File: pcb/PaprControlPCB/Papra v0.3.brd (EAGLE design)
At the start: 30 x 45 mm, 32 parts, among them Q1 AO3400A (C20917), U1 LP2985-50DBVR (C74511), U2 ATTINYX04SOIC14

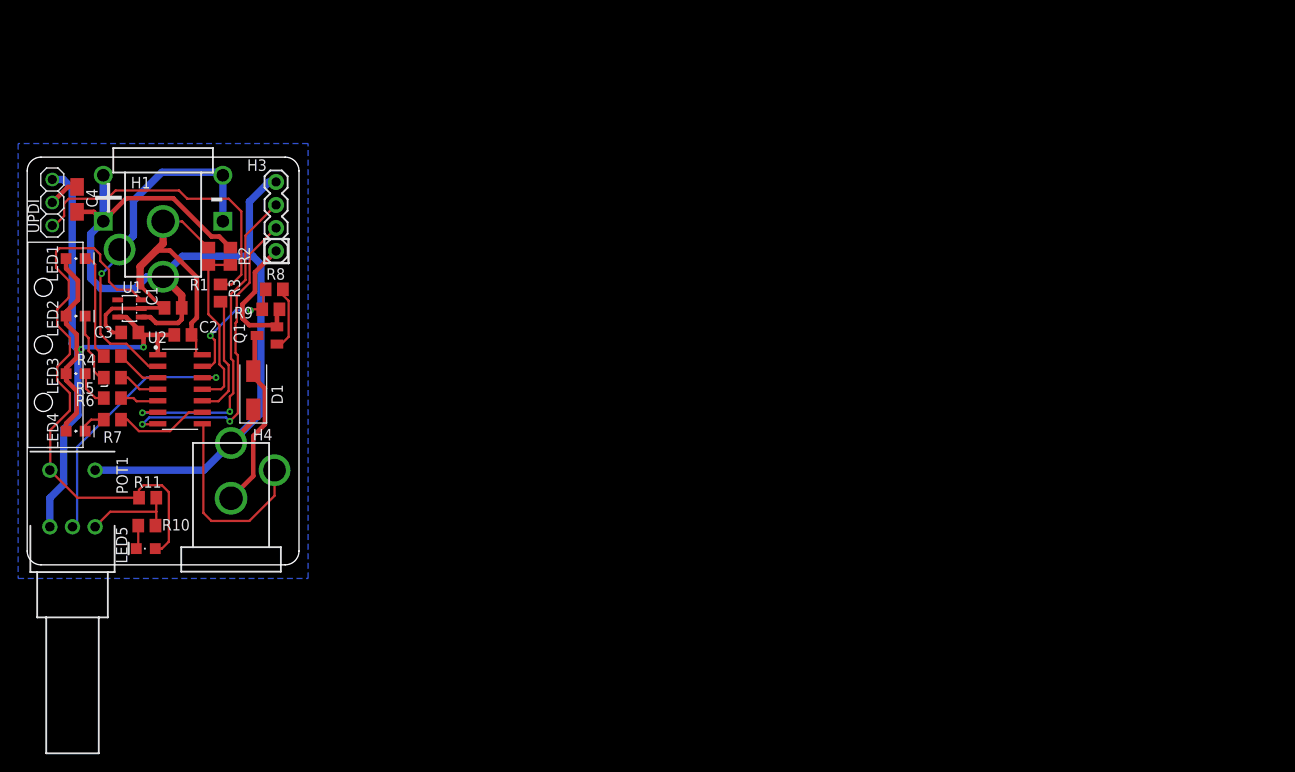
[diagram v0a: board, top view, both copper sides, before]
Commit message: Updating the boards for the 3rd build
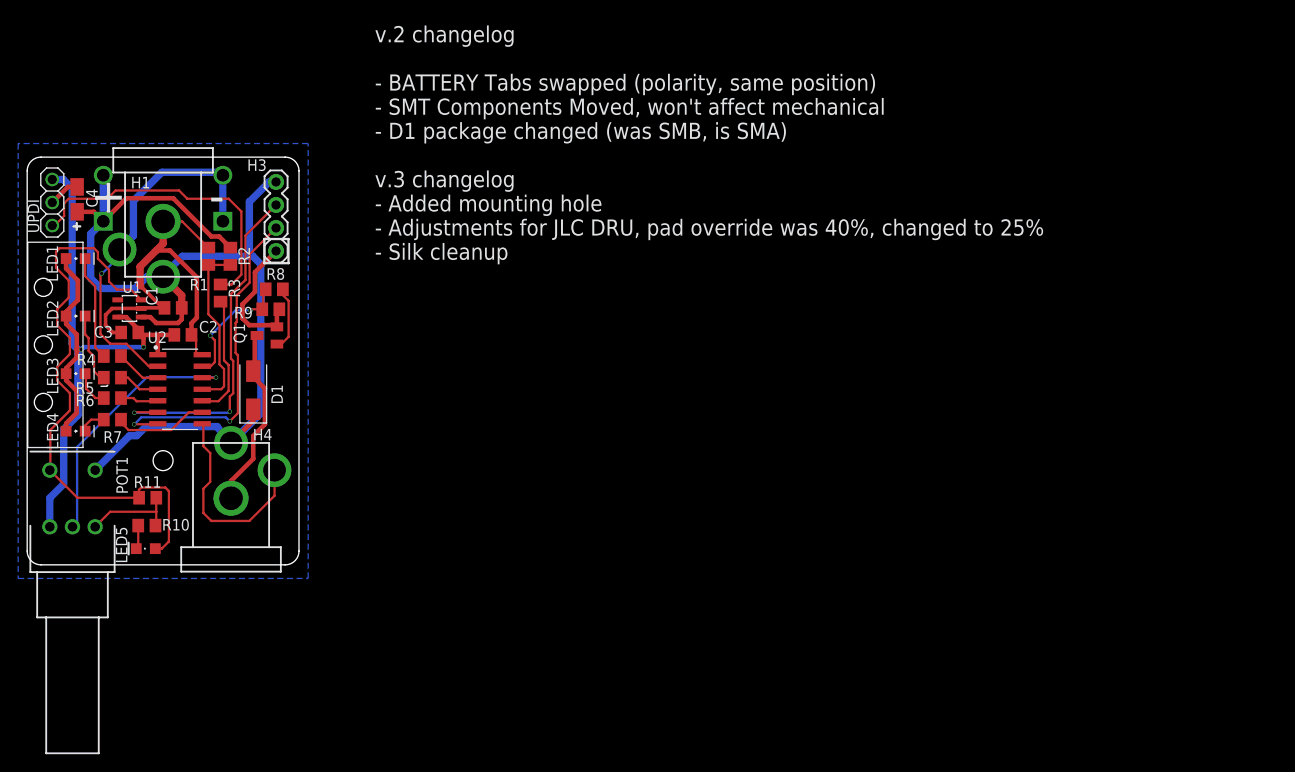
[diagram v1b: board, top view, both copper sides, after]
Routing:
- net EXPANSIONTX: track 35.6 -> 37.3 mm
- net EXPANSIONRX: track 36.6 -> 38.4 mm
- net +12V: track 116.3 -> 117.9 mm
- net FAN-SENSE: track 22.1 -> 22.7 mm
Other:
- board text added: "(C) 2021 TETRA BIO DISTRIBUTED"
- board text added: "15JAN2021"
- board text added: "PAPRA V0.3"
- board text added: "v.2 changelog - BATTERY Tabs swapped (polarity, same position) - SMT Components Moved, won't affect mechanical - D1 package changed (was SMB, is SMA) v.3 changelog - Added mounting hole - Adjustments for JLC DRU, pad override was 40%, changed to 25% - Silk cleanup"
- board text removed: "(C) 2020 TETRA BIO DISTRIBUTED"
- board text removed: "10DEC2020"
- board text removed: "PAPRA V0.2"
